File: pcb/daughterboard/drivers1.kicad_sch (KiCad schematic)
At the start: 17 parts, among them IC1 TLE94112ESXUMA1, IC2 TLE94112ESXUMA1, IC3 TLE94112ESXUMA1, IC4 TLE94112ESXUMA1

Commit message: addec electrolytic capacitors on 5v5 line
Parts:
- added C23: 220uF, A_HANU_FOOTPRINTS:EEE1AA101SP, symbol EEE0JA221WP:EEE0JA221WP
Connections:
- net +5.5V: now also C23.1 (+)
- net GND: now also C23.2 (-)

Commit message: added initial power lines
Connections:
- net SPI_MOSI: now also IC1.5 (SDI); no longer IC1.7 (SDO), IC2.5 (SDI)
- new net: IC1.7 (SDO), IC2.5 (SDI)

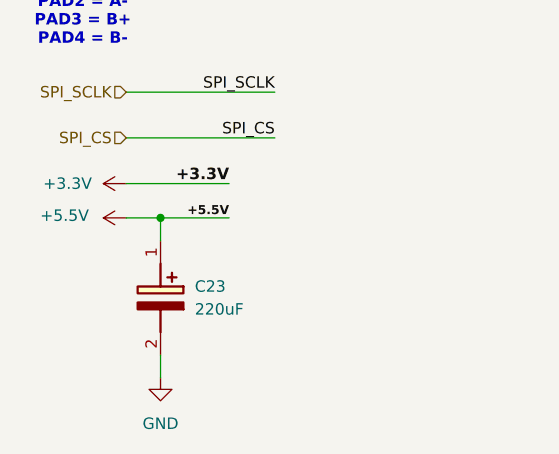
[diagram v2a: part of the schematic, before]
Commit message: Initial pcb design for daughterboard Added 3D models for components Modified the daughterboard to motherboard connectors Removed 220uF capacitors from the 5V5 power line
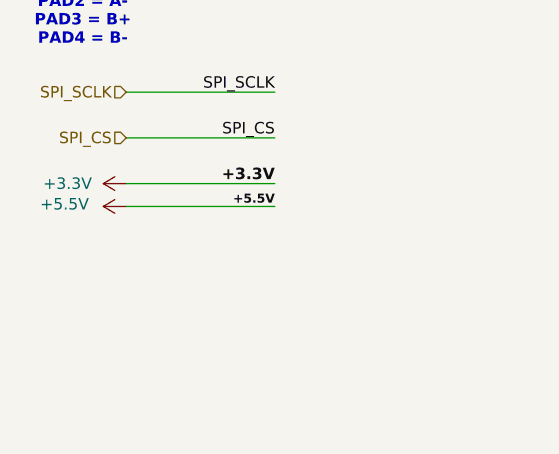
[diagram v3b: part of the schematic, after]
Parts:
- removed C23: 220uF, A_HANU_FOOTPRINTS:EEE1AA101SP, symbol EEE0JA221WP:EEE0JA221WP
- C1, C10, C11, C2, C4, C5, C7, C8: footprint A_HANU_FOOTPRINTS:CAPC0402X22N -> C0603C104K3RACAUTO:C0603
- C12, C3, C6, C9: footprint A_HANU_FOOTPRINTS:T491A -> LIB_T491A106K016AT:T491A

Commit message: Finalized daughterboard pcb design 0 errors Verified every 3D model, footprint According to the schematic
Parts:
- IC1, IC2, IC3, IC4: footprint A_HANU_FOOTPRINTS:TLE94112ESXUMA1 -> driver_tle:SOP65P600X115-25N
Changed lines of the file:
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@@
 			)
 		)
-		(property "Footprint" "A_HANU_FOOTPRINTS:TLE94112ESXUMA1"
+		(property "Footprint" "driver_tle:SOP65P600X115-25N"
 			(at 266.7 135.56 0)
 			(hide yes)
@@
 			)
 		)
-		(property "Footprint" "A_HANU_FOOTPRINTS:TLE94112ESXUMA1"
+		(property "Footprint" "driver_tle:SOP65P600X115-25N"
 			(at 71.12 135.56 0)
 			(hide yes)
@@
 			)
 		)
-		(property "Footprint" "A_HANU_FOOTPRINTS:TLE94112ESXUMA1"
+		(property "Footprint" "driver_tle:SOP65P600X115-25N"
 			(at 137.16 135.56 0)
 			(hide yes)
@@
 			)
 		)
-		(property "Footprint" "A_HANU_FOOTPRINTS:TLE94112ESXUMA1"
+		(property "Footprint" "driver_tle:SOP65P600X115-25N"
 			(at 200.66 135.56 0)
 			(hide yes)

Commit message: Final touches for the PCB order Added MPN, Description, checked footprints and 3D models Finished the BOM
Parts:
- C1, C10, C11, C2, C4, C5, C7, C8: Manufacturer_Name (none) -> KEMET; Manufacturer_Part_Number (none) -> C0603C104K3RACAUTO
- C12, C3, C6, C9: Manufacturer_Name (none) -> KEMET; Manufacturer_Part_Number (none) -> T491A106K016AT
- R1: Manufacturer_Name (none) -> Vishay; Manufacturer_Part_Number (none) -> CRCW060310K0FKEAHP
